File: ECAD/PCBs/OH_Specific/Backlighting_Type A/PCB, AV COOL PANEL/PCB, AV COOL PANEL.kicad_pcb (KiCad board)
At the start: 2 copper layers, 44.5 x 81.8 mm, 23 parts, among them J1 Conn_01x04_Female, J2 Conn_01x04_Female

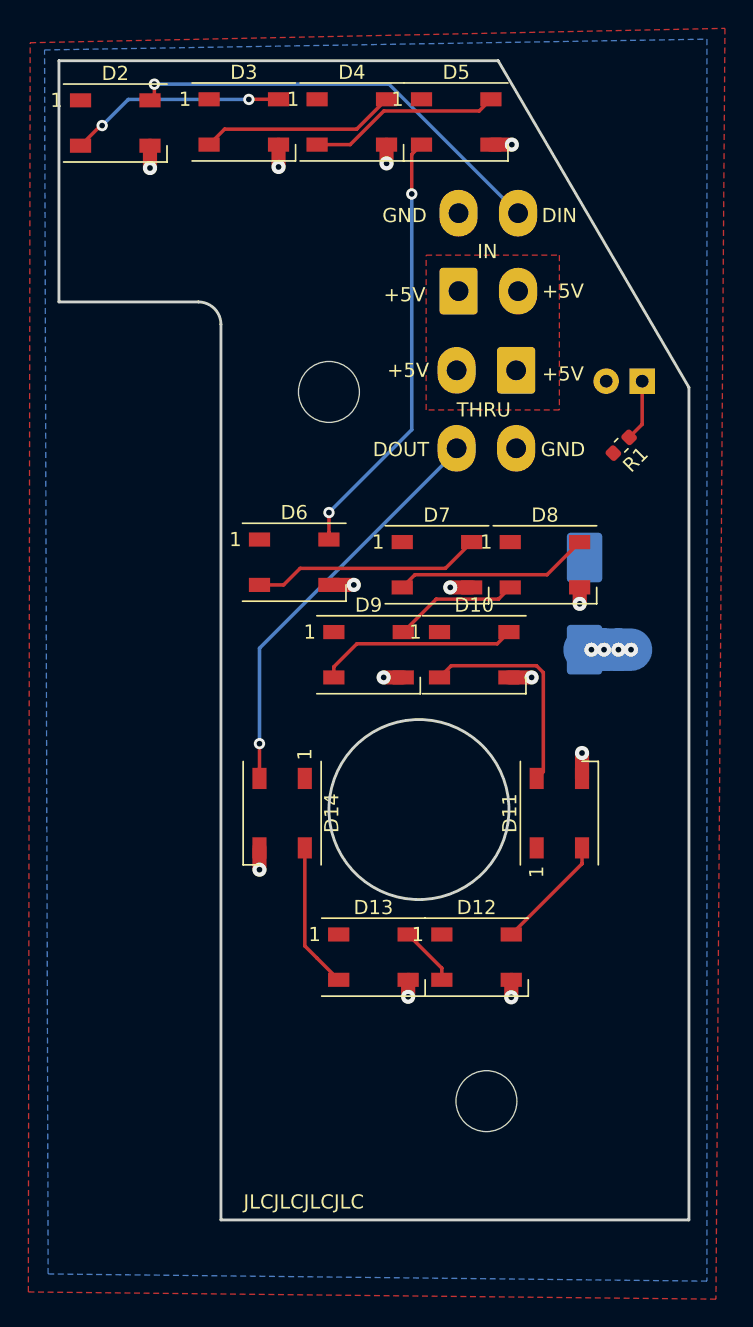
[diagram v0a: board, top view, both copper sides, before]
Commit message: Update: || KiCad 5 to 6 transition - AV COOL
AV COOL PANEL TRANSITION UPDATE
------------------------------------
1:  OH Nomenclature:  - Rename "AV COOL Panel" to "PCB, AV COOL PANEL"

2:  Added "Legacy" folder:  Used to store all files that are no longer being used and are associated with KiCad 5 and older.

3:  Removed old "AV COOL" BOM/CPL files:  Files were from APU Ver.1 that were parsed from a different plugin.  Outdated and no longer needed.

5:  Moved "fp-info-cache" to Legacy.:  "Cache to speed up loading of footprint libraries."  File is excess and not needed.  [Ref.:  https://docs.kicad.org/master/en/kicad/kicad.html

5:  Updated AV COOL Schematic:  - Fixed component footprint paths; Now point to OH_Footprints library.
-Molex Mini-Fit Jr.
-Generic Capacitor, Resisters, LEDs

6:  Updated APU Panel PCB:   - Fixed Logo footprint paths; now points to OH_Footprints.
-Molex Mini-Fit Jr.
-Generic Capacitor, Resisters, LEDs

***3d model's now properly display for PCB board.

7-Added new 3d images of PCB.

8: Updated JLC Manufacturing files:  - BOM_BOTTOM, BOM_TOP, & CPL.
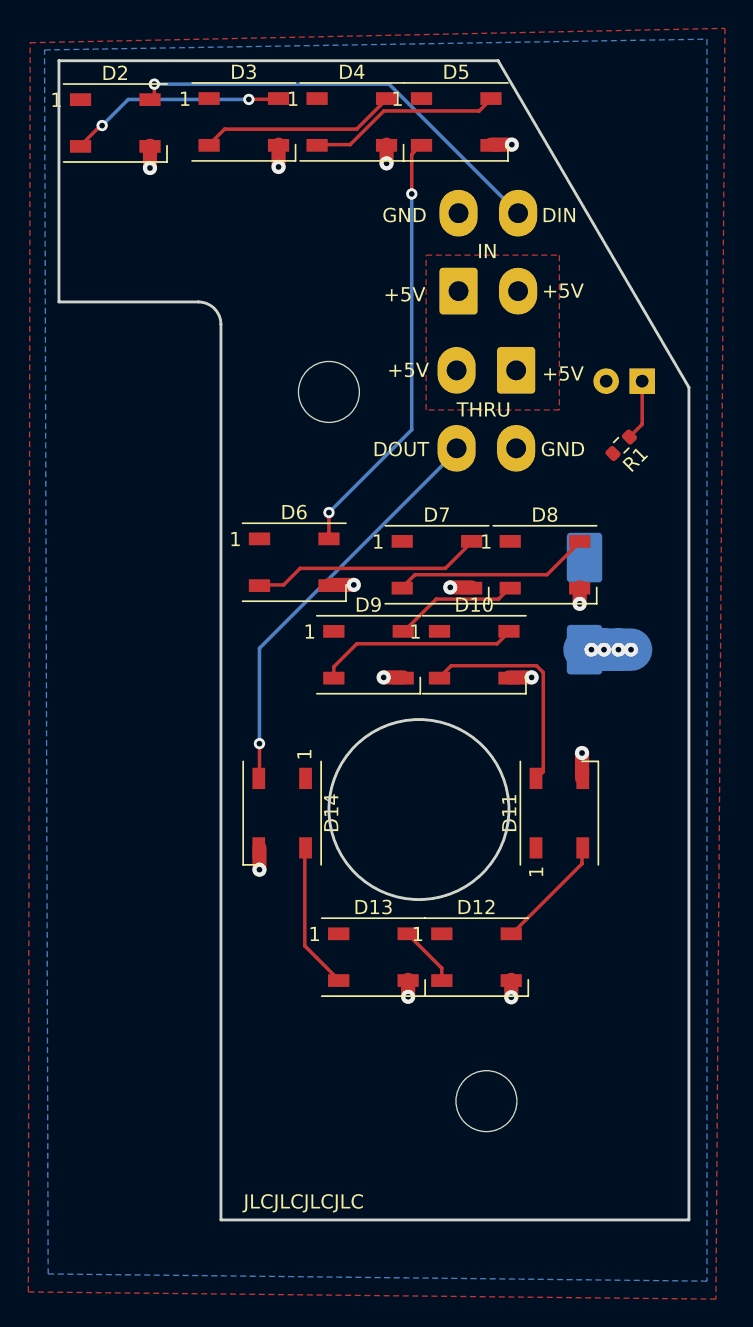
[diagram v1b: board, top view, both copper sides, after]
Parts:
- C1: footprint Capacitor_SMD:CP_Elec_8x10 -> OH_Footprints:CP_Elec_8x10
- D1: footprint LED_THT:LED_D3.0mm -> OH_Footprints:LED_D3.0mm
- D10, D11, D12, D13, D14, D2, D3, D4, D5, D6, D7, D8, D9: footprint LED_SMD:LED_WS2812B_PLCC4_5.0x5.0mm_P3.2mm -> OH_Footprints:LED_WS2812B_PLCC4_5.0x5.0mm_P3.2mm
- J1, J2: footprint Connector_Molex:Molex_Mini-Fit_Jr_5566-04A_2x02_P4.20mm_Vertical -> OH_Footprints:Molex_Mini-Fit_Jr_5566-04A_2x02_P4.20mm_Vertical
- R1: footprint Resistor_SMD:R_0603_1608Metric -> OH_Footprints:R_0603_1608Metric
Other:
- board text added: "Version 2.1"
- board text removed: "Version 2.0"
